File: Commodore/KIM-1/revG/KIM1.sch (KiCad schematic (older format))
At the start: 3 parts, among them U1 6502, U2 6530-002, U3 6530-003

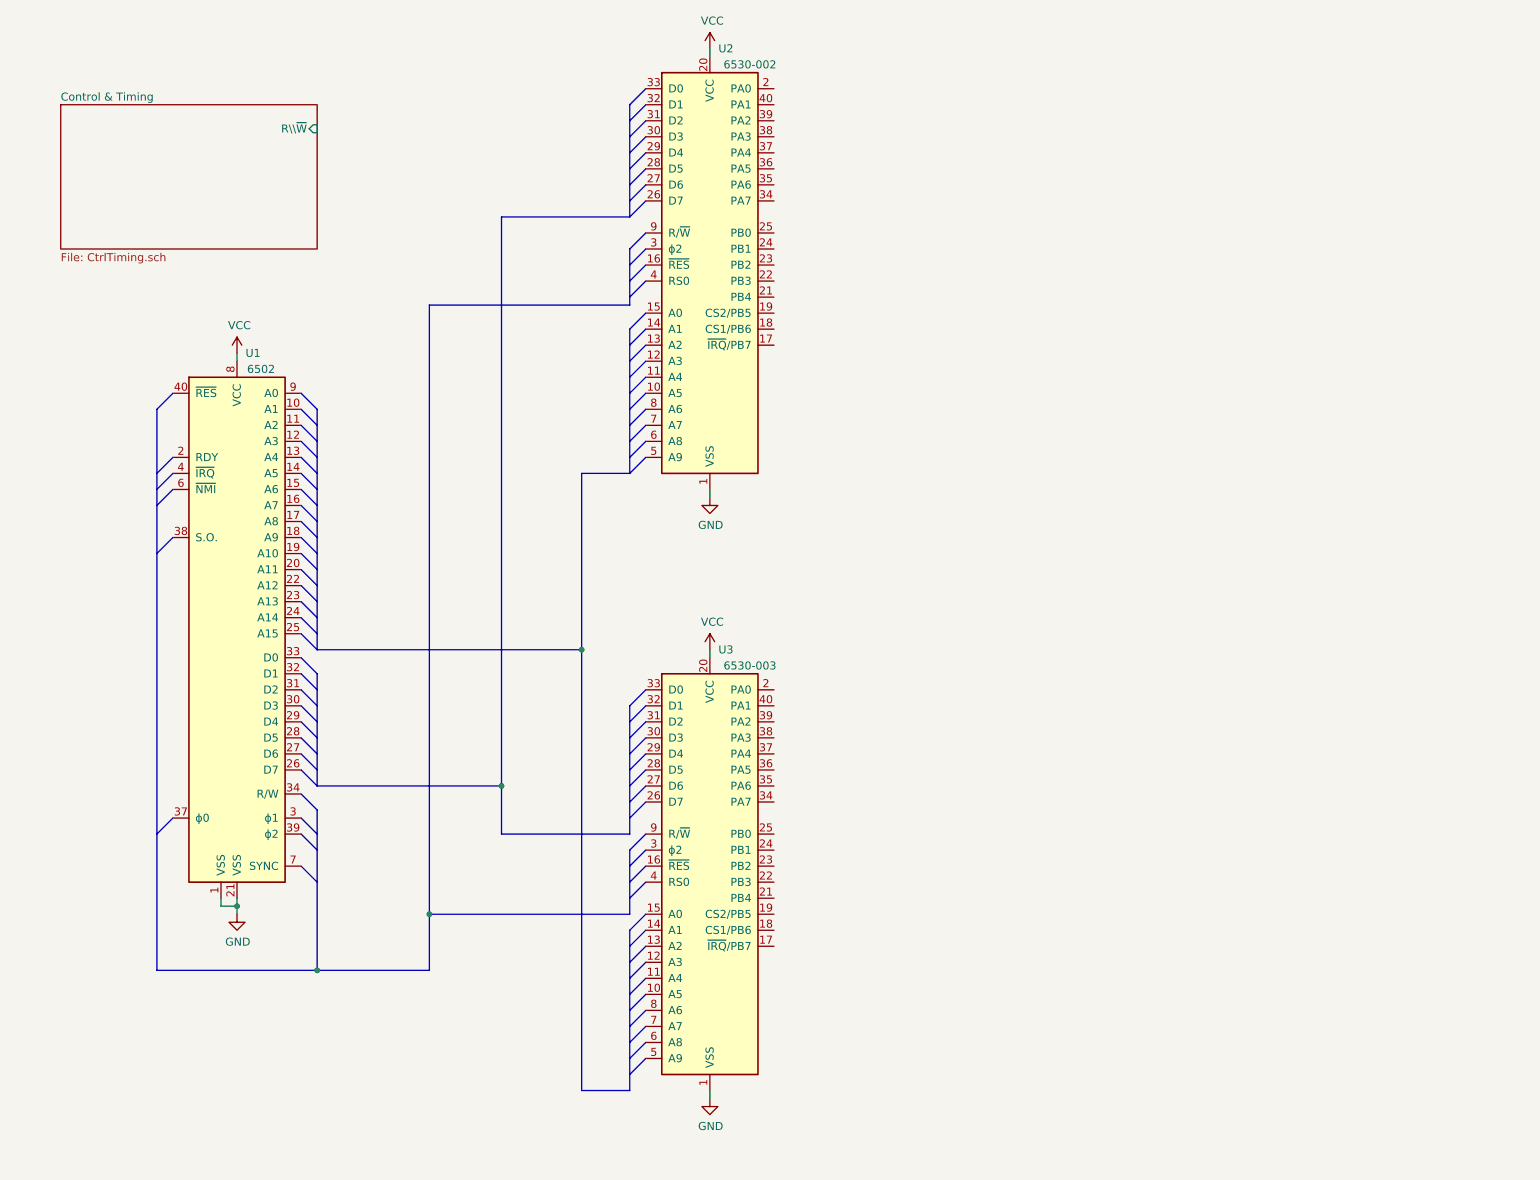
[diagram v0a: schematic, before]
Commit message: Schematic capture complete, todo: verify against reference system.
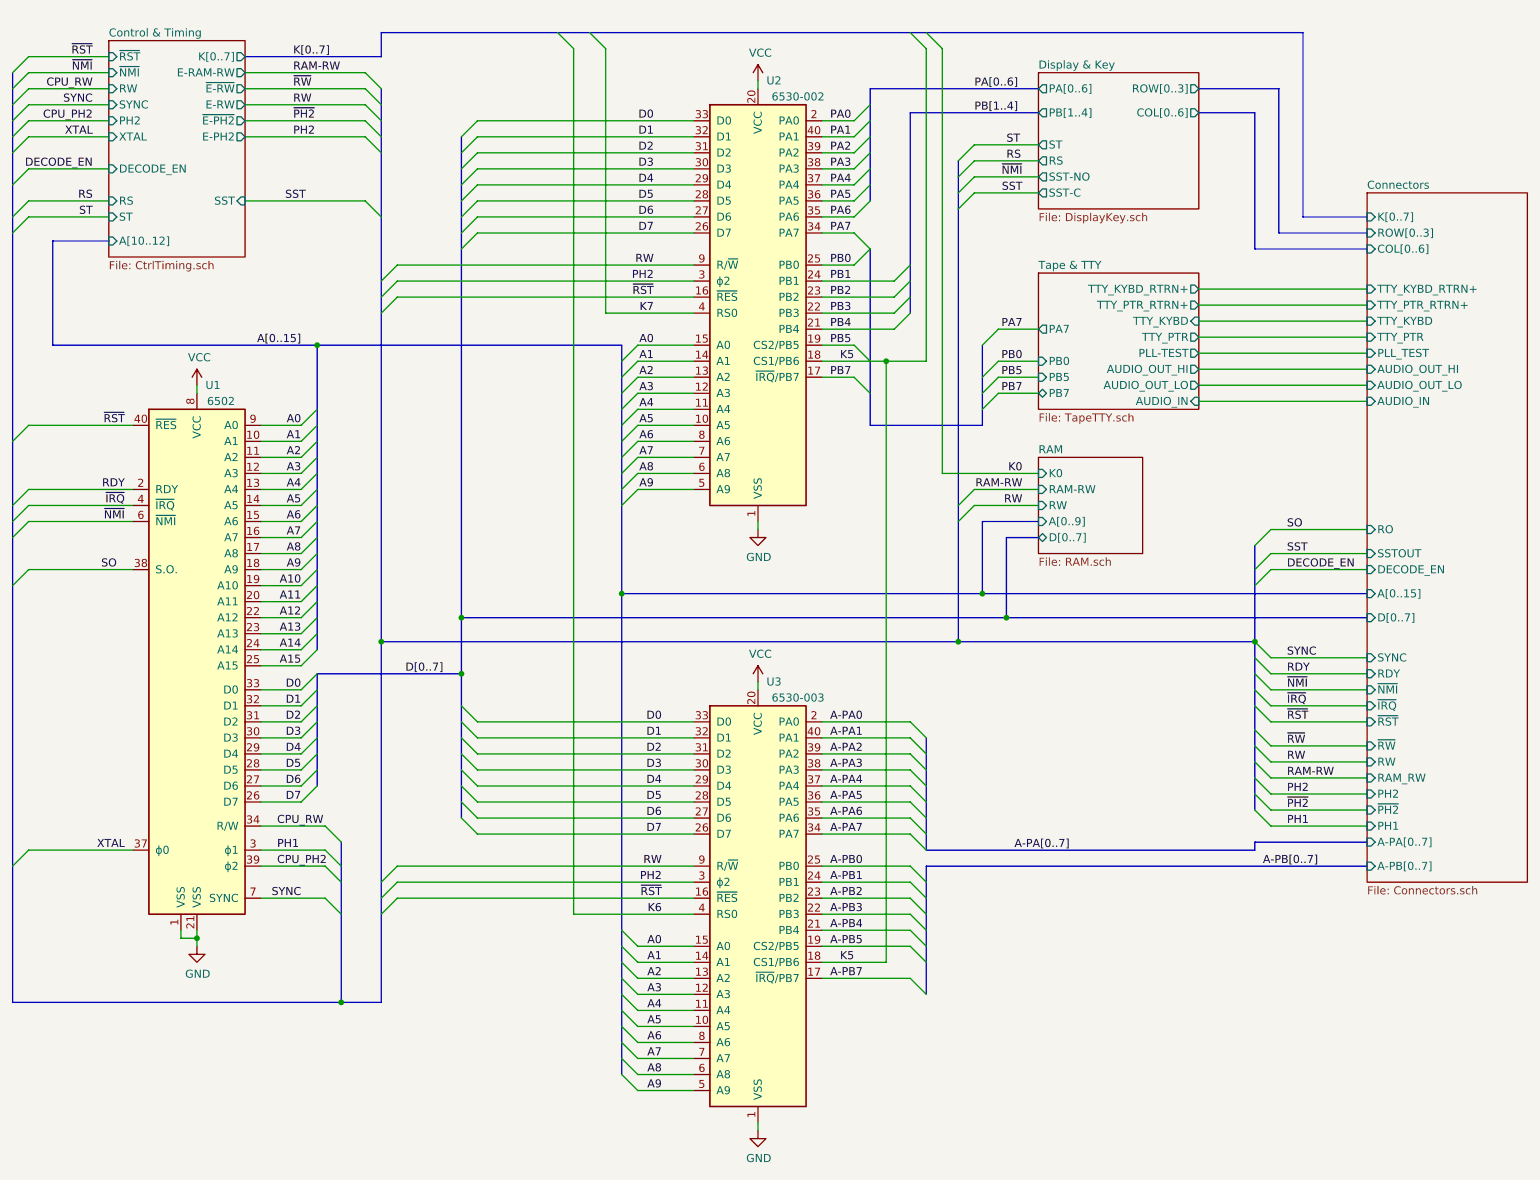
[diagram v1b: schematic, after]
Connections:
- net A1: now reaches U1.10 (A1)
- net A1: now also U2.14 (A1), U3.14 (A1)
- net A2: now reaches U1.11 (A2)
- net A2: now also U2.13 (A2), U3.13 (A2)
- net A3: now reaches U1.12 (A3)
- net A3: now also U2.12 (A3), U3.12 (A3)
- net A4: now reaches U1.13 (A4)
- net A4: now also U2.11 (A4), U3.11 (A4)
- net A5: now reaches U1.14 (A5)
- net A5: now also U2.10 (A5), U3.10 (A5)
- net A6: now reaches U1.15 (A6)
- net A6: now also U2.8 (A6), U3.8 (A6)
- net A7: now reaches U1.16 (A7)
- net A7: now also U2.7 (A7), U3.7 (A7)
- net A8: now reaches U1.17 (A8)
- net A8: now also U2.6 (A8), U3.6 (A8)
- net A9: now reaches U1.18 (A9)
- net A9: now also U2.5 (A9), U3.5 (A9)
- net A10: now reaches U1.19 (A10)
- net RDY: now reaches U1.2 (RDY)
- net A11: now reaches U1.20 (A11)
- net A12: now reaches U1.22 (A12)
- net A13: now reaches U1.23 (A13)
- net A14: now reaches U1.24 (A14)
- net A15: now reaches U1.25 (A15)
- net D7: now reaches U1.26 (D7)
- net D7: now also U2.26 (D7), U3.26 (D7)
- net D6: now reaches U1.27 (D6)
- net D6: now also U2.27 (D6), U3.27 (D6)
- net D5: now reaches U1.28 (D5)
- net D5: now also U2.28 (D5), U3.28 (D5)
- net D4: now reaches U1.29 (D4)
- net D4: now also U2.29 (D4), U3.29 (D4)
- net PH1: now reaches U1.3 (ϕ1)
- net D3: now reaches U1.30 (D3)
- net D3: now also U2.30 (D3), U3.30 (D3)
- net D2: now reaches U1.31 (D2)
- net D2: now also U2.31 (D2), U3.31 (D2)
- net D1: now reaches U1.32 (D1)
- net D1: now also U2.32 (D1), U3.32 (D1)
- net D0: now reaches U1.33 (D0)
- net D0: now also U2.33 (D0), U3.33 (D0)
- net CPU_RW: now reaches U1.34 (R/W)
- net XTAL: now reaches U1.37 (ϕ0)
- net SO: now reaches U1.38 (S.O.)
- net CPU_PH2: now reaches U1.39 (ϕ2)
- net ~IRQ: now reaches U1.4 (~IRQ)
- net ~RST: now reaches U1.40 (~RES)
- net ~RST: now also U2.16 (~RES), U3.16 (~RES)
- net ~NMI: now reaches U1.6 (~NMI)
- net SYNC: now reaches U1.7 (SYNC)
- net A0: now reaches U1.9 (A0)
- net A0: now also U2.15 (A0), U3.15 (A0)
- net A-PB7: now reaches U3.17 (~IRQ~/PB7)
- net K5: now reaches U3.18 (CS1/PB6)
- net K5: now also U2.18 (CS1/PB6)
- net A-PB5: now reaches U3.19 (CS2/PB5)
- net A-PA0: now reaches U3.2 (PA0)
- net A-PB4: now reaches U3.21 (PB4)
- net A-PB3: now reaches U3.22 (PB3)
- net A-PB2: now reaches U3.23 (PB2)
- net A-PB1: now reaches U3.24 (PB1)
- net A-PB0: now reaches U3.25 (PB0)
- net PH2: now reaches U3.3 (ϕ2)
- net PH2: now also U2.3 (ϕ2)
- net A-PA7: now reaches U3.34 (PA7)
- net A-PA6: now reaches U3.35 (PA6)
- net A-PA5: now reaches U3.36 (PA5)
- net A-PA4: now reaches U3.37 (PA4)
- net A-PA3: now reaches U3.38 (PA3)
- net A-PA2: now reaches U3.39 (PA2)
- net K6: now reaches U3.4 (RS0)
- net A-PA1: now reaches U3.40 (PA1)
- net RW: now reaches U3.9 (R/~W)
- net RW: now also U2.9 (R/~W)
- net PB7: now reaches U2.17 (~IRQ~/PB7)
- net PB5: now reaches U2.19 (CS2/PB5)
- net PA0: now reaches U2.2 (PA0)
- net PB4: now reaches U2.21 (PB4)
- net PB3: now reaches U2.22 (PB3)
- net PB2: now reaches U2.23 (PB2)
- net PB1: now reaches U2.24 (PB1)
- net PB0: now reaches U2.25 (PB0)
- net PA7: now reaches U2.34 (PA7)
- net PA6: now reaches U2.35 (PA6)
- net PA5: now reaches U2.36 (PA5)
- net PA4: now reaches U2.37 (PA4)
- net PA3: now reaches U2.38 (PA3)
- net PA2: now reaches U2.39 (PA2)
- net K7: now reaches U2.4 (RS0)
- net PA1: now reaches U2.40 (PA1)
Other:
- moved on the sheet: U1, U2, U3

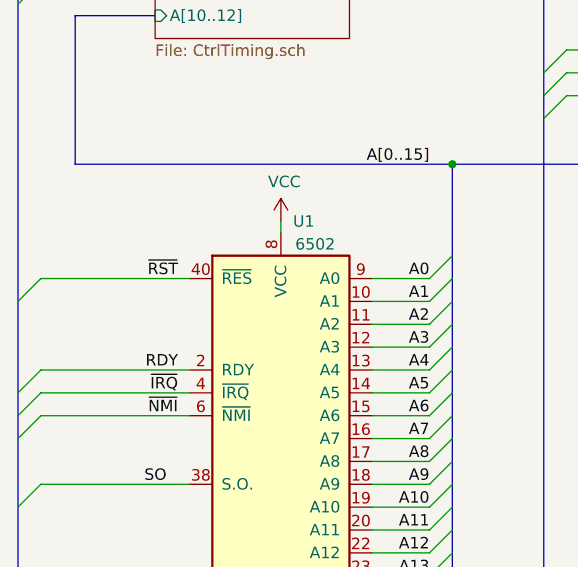
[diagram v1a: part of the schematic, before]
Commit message: Fixed missing/wrong designators, keypad labeling between sheets, PA & PB routing between sheets.
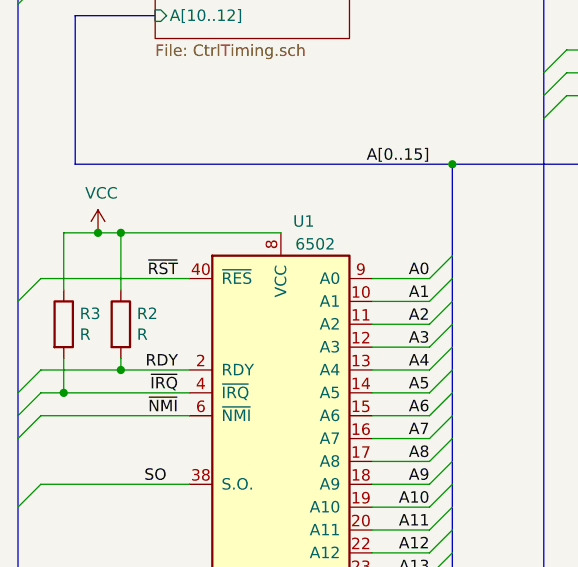
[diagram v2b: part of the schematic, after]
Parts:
- added R2, R3: R, symbol Device:R
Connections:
- net RDY: now also R2.2
- net VCC: now also R2.1, R3.1
- net ~IRQ: now also R3.2
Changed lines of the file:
@@
 L power:VCC #PWR0101
 U 1 1 60C34E8A
-P 2150 2850
-F 0 "#PWR0101" H 2150 2700 50  0001 C CNN
-F 1 "VCC" H 2165 3023 50  0000 C CNN
-F 2 "" H 2150 2850 50  0001 C CNN
-F 3 "" H 2150 2850 50  0001 C CNN
-	1    2150 2850
+P 1350 2900
+F 0 "#PWR0101" H 1350 2750 50  0001 C CNN
+F 1 "VCC" H 1365 3073 50  0000 C CNN
+F 2 "" H 1350 2900 50  0001 C CNN
+F 3 "" H 1350 2900 50  0001 C CNN
+	1    1350 2900
 	1    0    0    -1
 $EndComp
 Wire Wire Line
-	2150 2850 2150 2900
+	1350 2900 1450 2900
 $Comp
 L power:VCC #PWR0102
@@
 	1000 3800 1100 3700
 Wire Wire Line
-	1100 3500 1750 3500
-Wire Wire Line
-	1100 3600 1750 3600
+	1100 3500 1450 3500
+Wire Wire Line
+	1100 3600 1200 3600
 Wire Wire Line
 	1100 3700 1750 3700
@@
 Text Label 7000 1000 0    50   ~ 0
 PA[0..6]
+$Comp
+L Device:R R3
+U 1 1 60CC7385
+P 1200 3300
+F 0 "R3" H 1270 3346 50  0000 L CNN
+F 1 "R" H 1270 3255 50  0000 L CNN
+F 2 "" V 1130 3300 50  0001 C CNN
+F 3 "~" H 1200 3300 50  0001 C CNN
+	1    1200 3300
+	1    0    0    -1
+$EndComp
+$Comp
+L Device:R R2
+U 1 1 60CCA44A
+P 1450 3300
+F 0 "R2" H 1520 3346 50  0000 L CNN
+F 1 "R" H 1520 3255 50  0000 L CNN
+F 2 "" V 1380 3300 50  0001 C CNN
+F 3 "~" H 1450 3300 50  0001 C CNN
+	1    1450 3300
+	1    0    0    -1
+$EndComp
+Wire Wire Line
+	1200 3450 1200 3600
+Connection ~ 1200 3600
+Wire Wire Line
+	1200 3600 1750 3600
+Wire Wire Line
+	1450 3450 1450 3500
+Connection ~ 1450 3500
+Wire Wire Line
+	1450 3500 1750 3500
+Wire Wire Line
+	1450 3150 1450 2900
+Connection ~ 1450 2900
+Wire Wire Line
+	1450 2900 2150 2900
+Wire Wire Line
+	1350 2900 1200 2900
+Wire Wire Line
+	1200 2900 1200 3150
 Wire Wire Line
 	6050 2700 6450 2700
@@
 Wire Bus Line
 	2900 2600 2900 4500
+Connection ~ 1350 2900
 $EndSCHEMATC

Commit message: Updated component values.
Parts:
- R2: renamed from R3; value R -> 3.3K
- R3: renamed from R2; value R -> 3.3K
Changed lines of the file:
@@
 Wire Wire Line
 	7400 1650 7000 1650
+Text Label 7300 1550 2    50   ~ 0
+SST
 Text Label 7300 1650 2    50   ~ 0
-SST
-Text Label 7300 1550 2    50   ~ 0
 ~NMI
 Entry Wire Line
@@
 PA[0..6]
 $Comp
-L Device:R R3
+L Device:R R2
 U 1 1 60CC7385
 P 1200 3300
-F 0 "R3" H 1270 3346 50  0000 L CNN
-F 1 "R" H 1270 3255 50  0000 L CNN
+F 0 "R2" H 1270 3346 50  0000 L CNN
+F 1 "3.3K" H 1270 3255 50  0000 L CNN
 F 2 "" V 1130 3300 50  0001 C CNN
 F 3 "~" H 1200 3300 50  0001 C CNN
@@
 $EndComp
 $Comp
-L Device:R R2
+L Device:R R3
 U 1 1 60CCA44A
 P 1450 3300
-F 0 "R2" H 1520 3346 50  0000 L CNN
-F 1 "R" H 1520 3255 50  0000 L CNN
+F 0 "R3" H 1520 3346 50  0000 L CNN
+F 1 "3.3K" H 1520 3255 50  0000 L CNN
 F 2 "" V 1380 3300 50  0001 C CNN
 F 3 "~" H 1450 3300 50  0001 C CNN
@@
 Wire Wire Line
 	1200 2900 1200 3150
+Connection ~ 1350 2900
 Wire Wire Line
 	6050 2700 6450 2700
@@
 Wire Bus Line
 	2900 2600 2900 4500
-Connection ~ 1350 2900
 $EndSCHEMATC

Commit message: Move KIM specific components out of shared libraries into the project library
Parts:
- U2, U3: symbol Interface_Expansion_MOSTechnology:6530 -> Kim1:6530
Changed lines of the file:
@@
 $EndDescr
 $Comp
-L Interface_Expansion_MOSTechnology:6530 U3
+L Kim1:6530 U3
 U 1 1 60C043D6
 P 5650 6050
@@
 $EndComp
 $Comp
-L Interface_Expansion_MOSTechnology:6530 U2
+L Kim1:6530 U2
 U 1 1 60C0A4B5
 P 5650 2300
